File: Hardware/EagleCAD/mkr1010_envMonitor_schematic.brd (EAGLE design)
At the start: 85.1 x 59.4 mm, 6 parts, among them J1 SGP30, J2 PMSA003I, J3 MEMS MIC, J4 TEST_POINTS, J5 RESET, U1 ARDUINO_MKR_ZERO

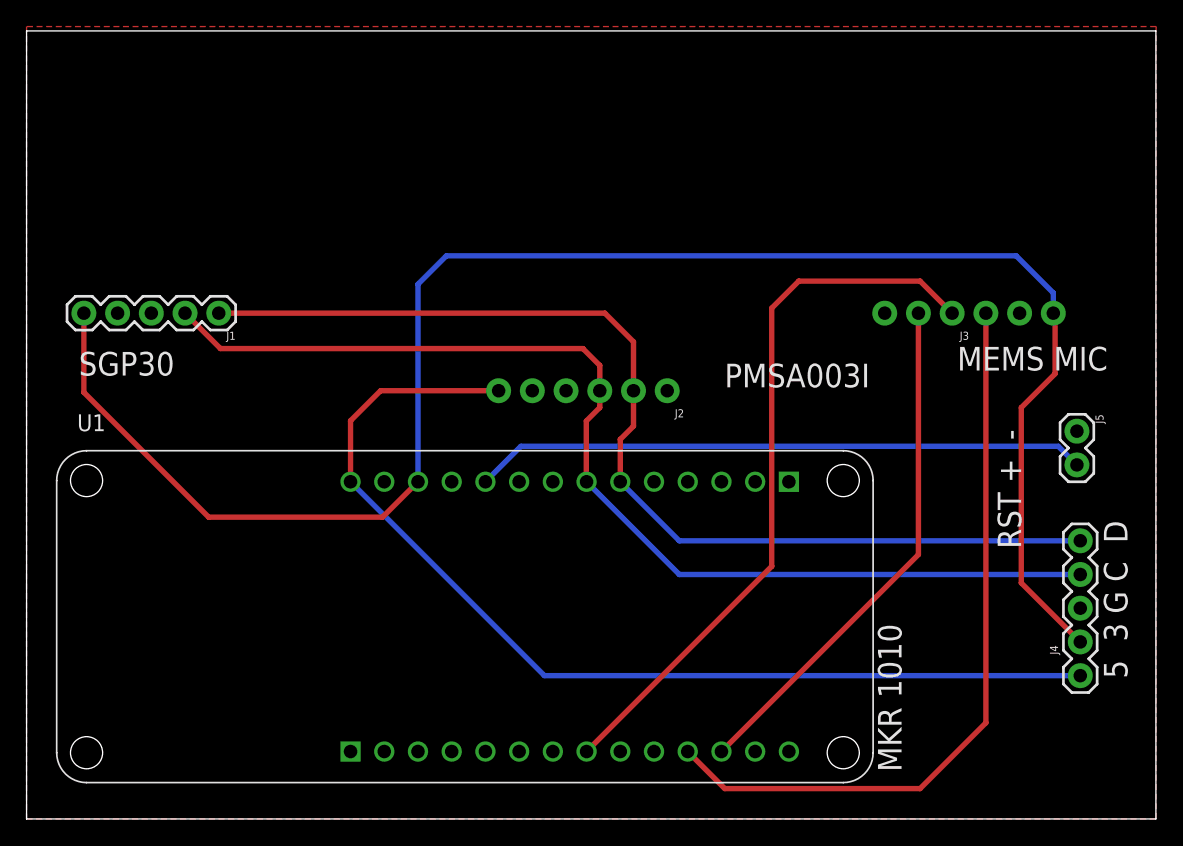
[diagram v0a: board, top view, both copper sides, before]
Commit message: Corrected PMSA003I board layout (6pin vs 7pin header)
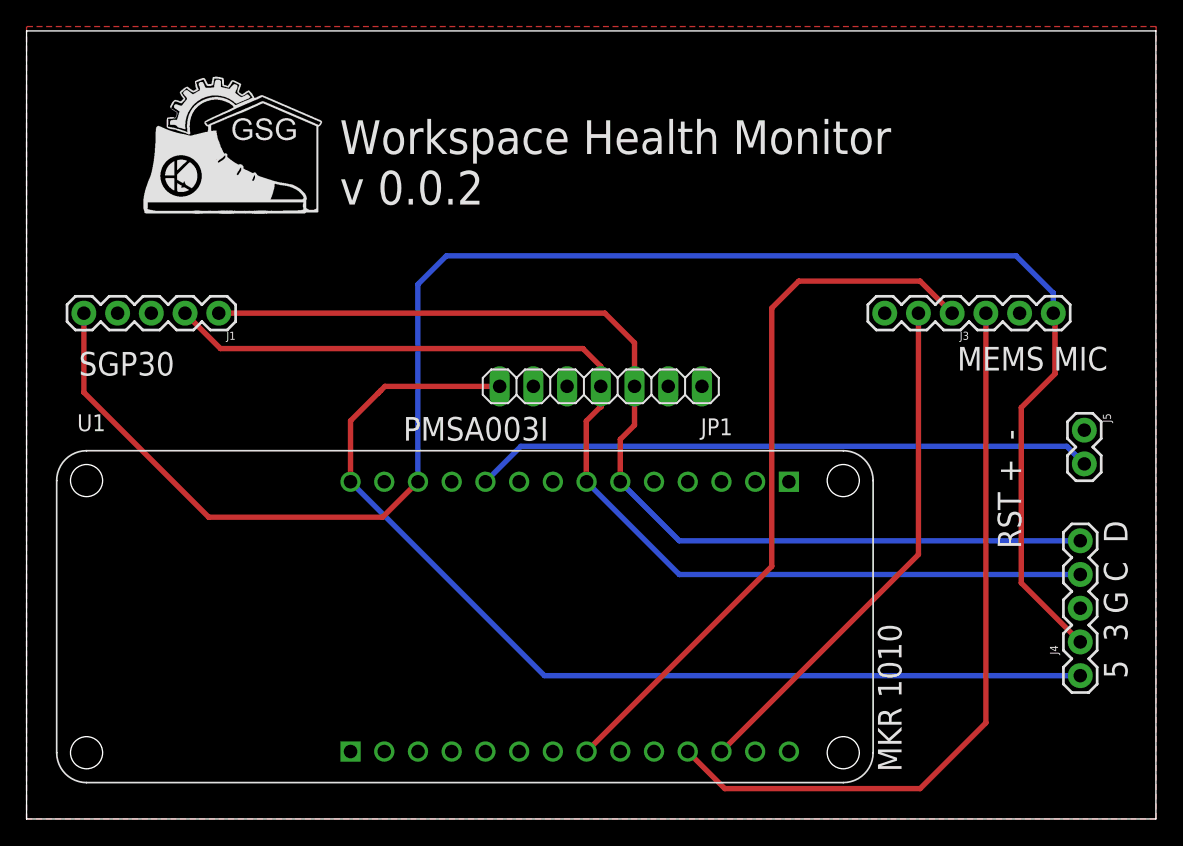
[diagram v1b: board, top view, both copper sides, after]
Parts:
- removed J2: PMSA003I, SparkFun-Connectors:1X06_NO_SILK
- added JP1: PMSA003I, pinhead:1X07
- J3: device SparkFun-Connectors:1X06_NO_SILK -> SparkFun-Connectors:1X06
- moved J5 0.56 mm to (79.7, 29.3)
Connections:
- net 5V: now also JP1.7; no longer J2.6
- net GND: now also JP1.5; no longer J2.4
- net SCL: now also JP1.4; no longer J2.3
- net SDA: now also JP1.3; no longer J2.2
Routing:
- net RESET: track 46.2 -> 46.8 mm
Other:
- board text added: "C:/Users/mpark/OneDrive/My Documents/Green Shoe Garage/GSG Images/GSG_BW.bmp"
- board text added: "Green Shoe Garage Workspace Health Monitor v. 0.0.2 14OCT2020"
- board text added: "Workspace Health Monitor v 0.0.2"
- board text removed: "Green Shoe Garage Workspace Health Monitor v. 0.0.1 11OCT2020"
